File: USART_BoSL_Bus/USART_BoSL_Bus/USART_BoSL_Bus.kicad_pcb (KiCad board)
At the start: 2 copper layers, 41.5 x 17.3 mm, 8 parts, among them J1 6P6C, J2 Conn_01x06, J3 Conn_01x08, J4 Conn_01x08, U1 SN65HVD75

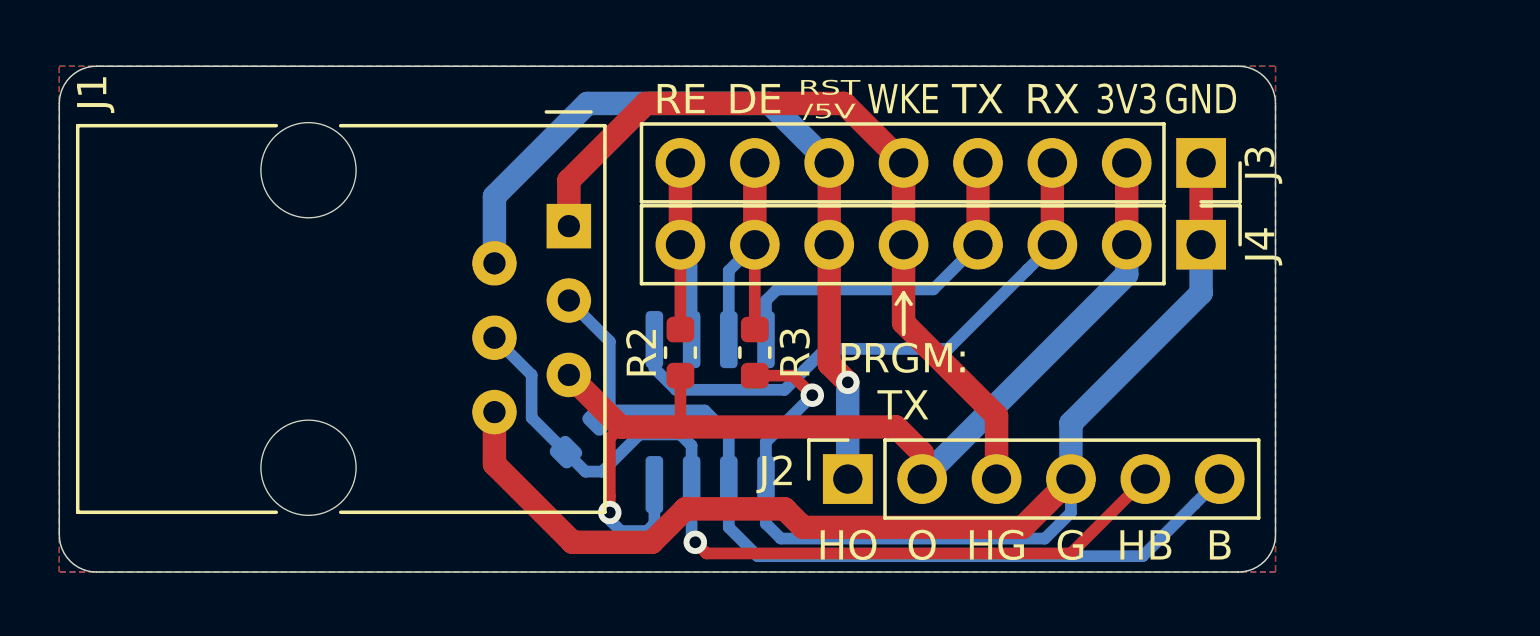
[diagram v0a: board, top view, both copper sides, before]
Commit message: added rev 0.1.1 of bosl bus converter, replaced pin headers for screw terminasl and hanging wires
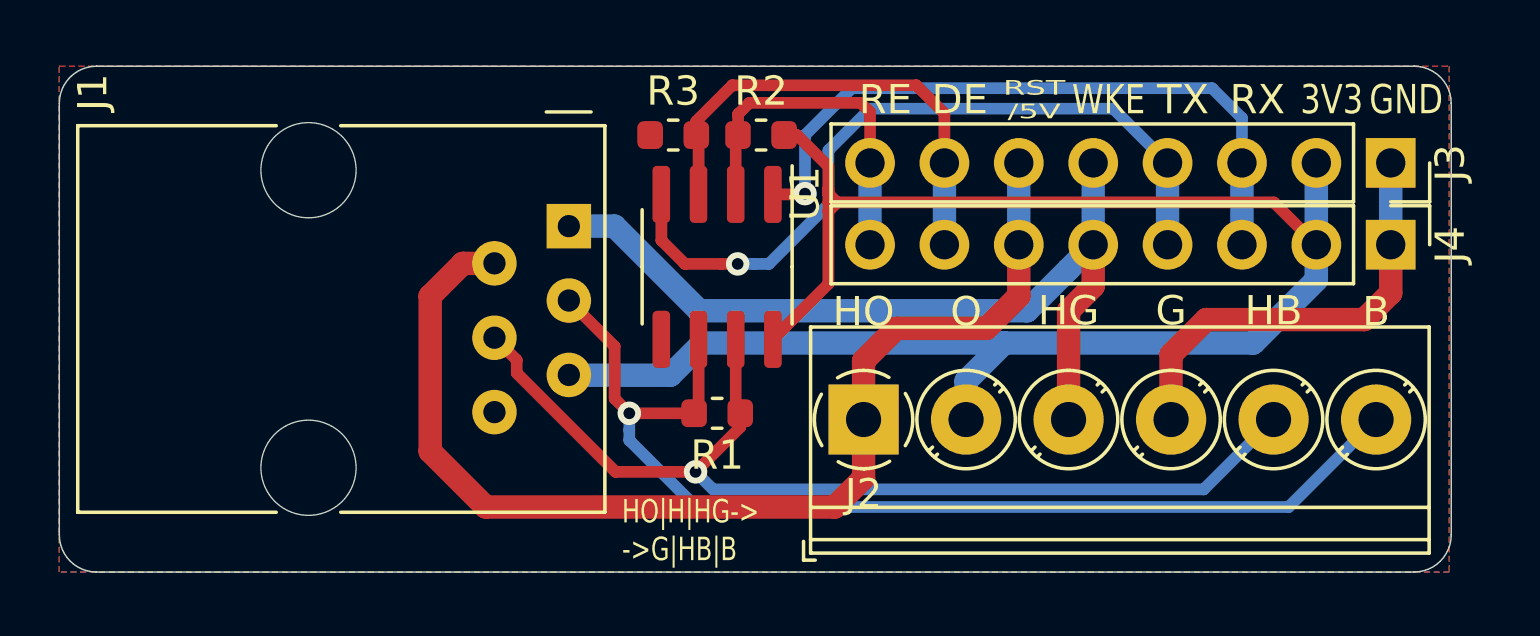
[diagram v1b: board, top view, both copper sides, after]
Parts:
- J2: value Conn_01x06 -> Screw_Terminal_01x06; footprint Connector_PinSocket_2.54mm:PinSocket_1x06_P2.54mm_Vertical -> TerminalBlock_Phoenix:TerminalBlock_Phoenix_PT-1,5-6-3.5-H_1x06_P3.50mm_Horizontal
- R1, U1: moved to F.Cu
- moved R3 7.93 mm to (126.5, 115.0), turned to 0 degrees
- moved R2 7.92 mm to (129.5, 115.0), turned to 0 degrees
- moved J3 6.47 mm to (151.0, 116.0)
- moved J4 6.47 mm to (151.0, 118.7)
- moved U1 4.97 mm to (128.0, 119.5)
- moved R1 4.67 mm to (128.0, 124.5), turned to 180 degrees
- moved J2 2.10 mm to (133.0, 124.7), turned to 0 degrees
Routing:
- net GREEN: track 56.0 -> 15.0 mm, vias 1 -> 0
- net ORANGE: track 36.0 -> 61.0 mm, vias 1 -> 0
- net TX: track 12.2 -> 26.0 mm, vias 0 -> 1
- net H_ORANGE: track 26.9 -> 38.7 mm, vias 1 -> 0
- net DE: track 9.30 -> 16.4 mm
- net BLUE: track 31.1 -> 38.1 mm, vias 0 -> 1
- net H_BLUE: track 30.1 -> 35.2 mm
- net RX: track 19.7 -> 23.4 mm, vias 0 -> 1
- net RE: track 9.09 -> 12.1 mm
- net H_GREEN: track 27.0 -> 29.1 mm
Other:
- board size 41.5 x 17.3 mm -> 47.5 x 17.3 mm
- board text added: "BoSL Bus rev 0.1.1"
- board text added: "HO|H|HG-> ->G|HB|B"
- board text added: "PGRM: TX"
- board text removed: "BoSL Bus rev 0.1.0"
- board text removed: "PRGM: TX"
